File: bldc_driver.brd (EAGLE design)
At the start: 48 x 30 mm, 42 parts, among them Q1 MOSFET-N, Q2 MOSFET-N, Q3 MOSFET-N, Q4 MOSFET-N, Q5 MOSFET-N, Q6 MOSFET-N, X1 LOGIC, X3 MICROMATCH-10

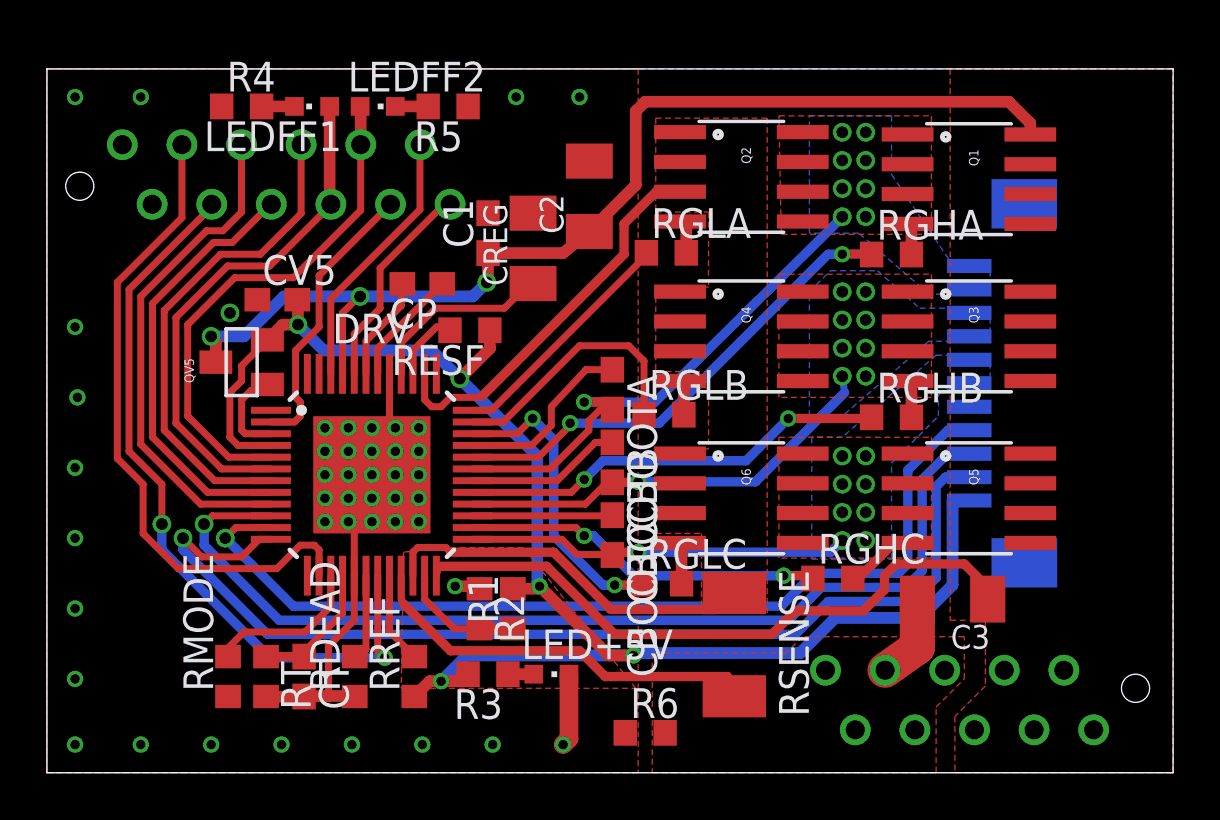
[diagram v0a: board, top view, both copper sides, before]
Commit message: Changed hall sensor connections to proper order
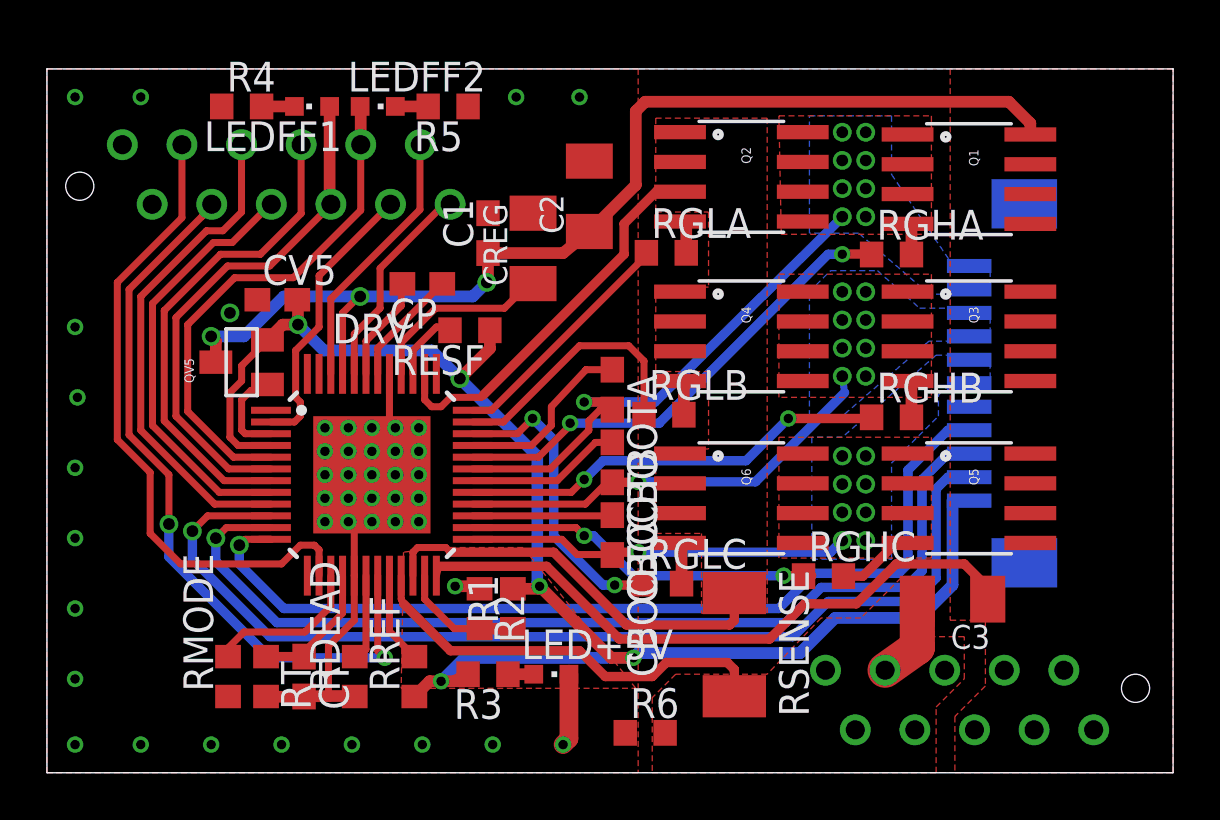
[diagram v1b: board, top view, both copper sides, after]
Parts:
- moved RGHC 0.41 mm to (33.1, 8.38)
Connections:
- net H1: now also MOTOR.10; no longer MOTOR.9
- net H2: now also MOTOR.9; no longer MOTOR.8
- net H3: now also MOTOR.8; no longer MOTOR.10
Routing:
- net H3: track 45.0 -> 40.1 mm
- net H2: track 40.5 -> 42.0 mm
- net H1: track 43.1 -> 44.3 mm
- net LSS: track 32.9 -> 34.2 mm
- net GNDA: track 20.9 -> 21.9 mm
